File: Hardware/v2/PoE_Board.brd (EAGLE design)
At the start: 84.6 x 72.1 mm, 93 parts, among them U1 EDISON_CONNECTOR_FULLMOUNTING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, U2 LAN9512-JZX, U3 MAX4995AAUT+, U4 EDISON_CONNECTOR_FULLHEADER

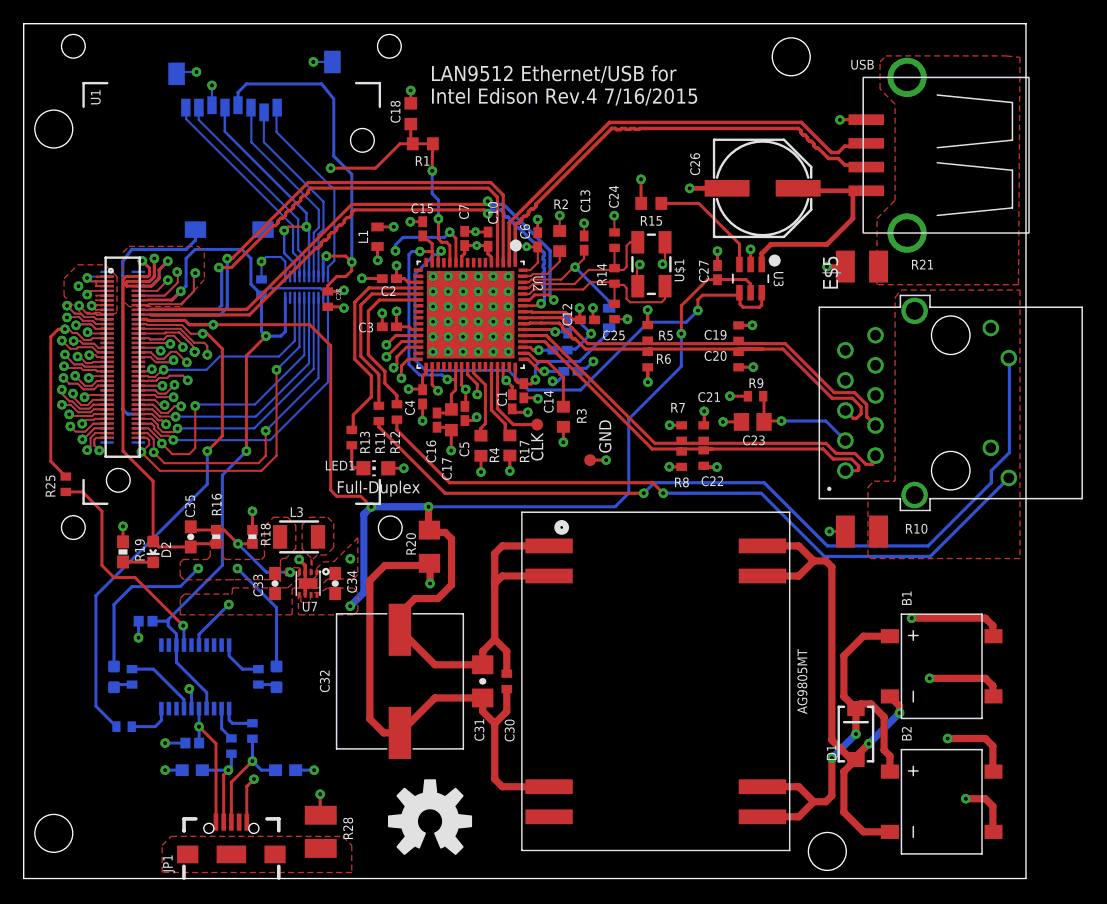
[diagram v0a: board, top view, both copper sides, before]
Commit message: Fixed part labels, fixed a couple acute angles
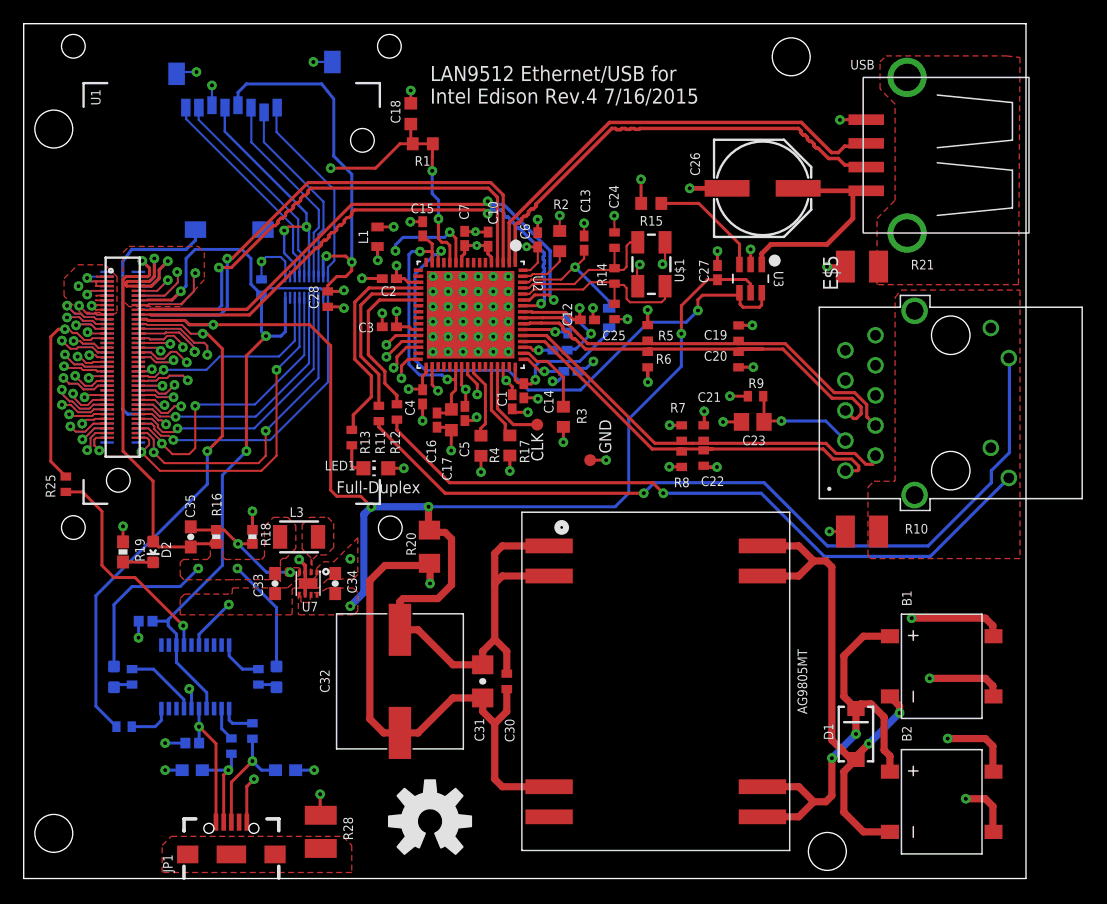
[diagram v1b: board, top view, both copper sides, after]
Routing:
- net USB_VBUS: track 143.4 -> 144.0 mm
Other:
- board text added: "RX"
- board text added: "TX"
